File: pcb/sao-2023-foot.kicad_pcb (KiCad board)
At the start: 2 copper layers, 38.1 x 71.9 mm, 6 parts, among them J1 Conn_02x03_Odd_Even

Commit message: Now with KUBERNETES!
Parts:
- removed the G*** at (148.6, 95.2)
- added G***: LOGO, sao-2023-foot:foot_outline_edge, F.Cu at (148.6, 95.1)
- added G***: LOGO, sao-2023-foot:toes, F.Cu at (148.6, 95.0)
- moved R1 1.09 mm to (145.1, 95.0)
- moved D1 0.26 mm to (147.9, 78.3)
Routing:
- net 3V3: track 0.00 -> 22.0 mm
- net Net-(D1-A): track 0.00 -> 15.2 mm
- added copper zone on B.Cu, net GND
- added copper zone on F.Cu, net GND
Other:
- outline, holes or cut-outs redrawn

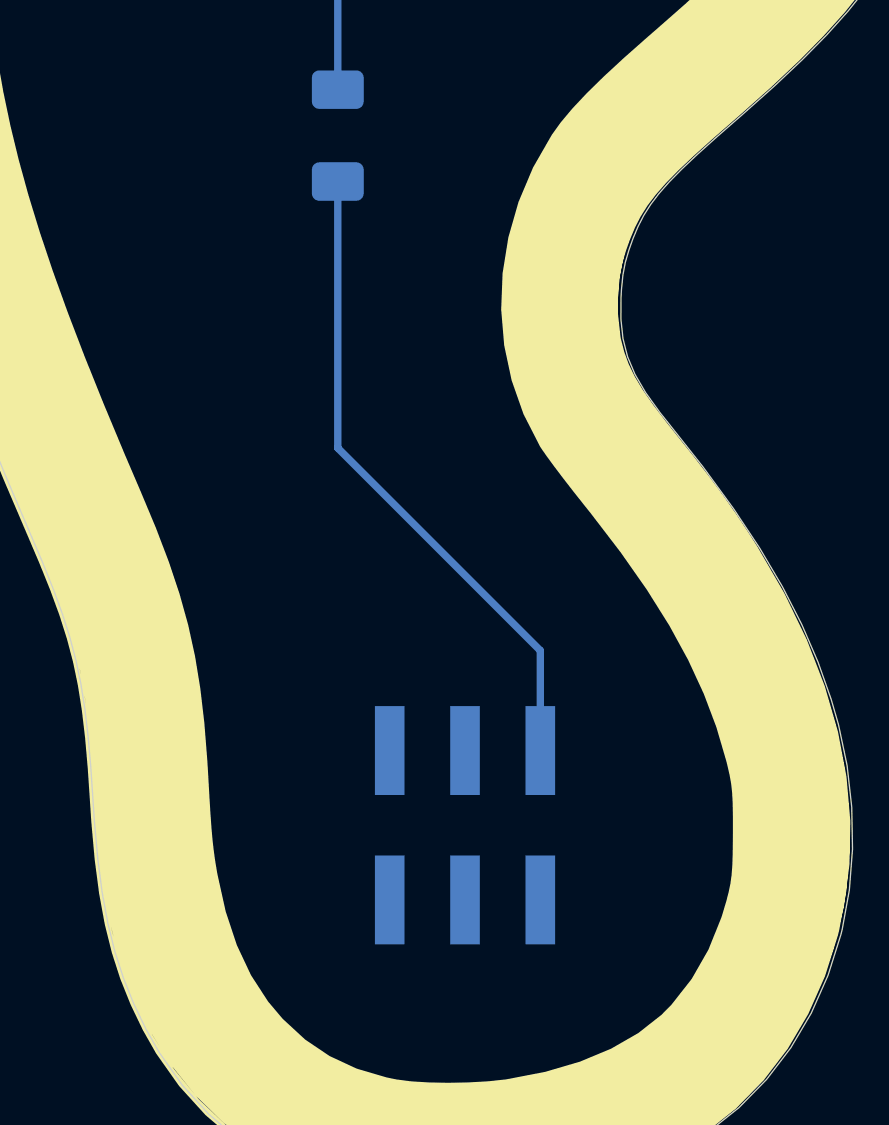
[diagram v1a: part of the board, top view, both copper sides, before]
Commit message: Corrected SAO Connector (#4)
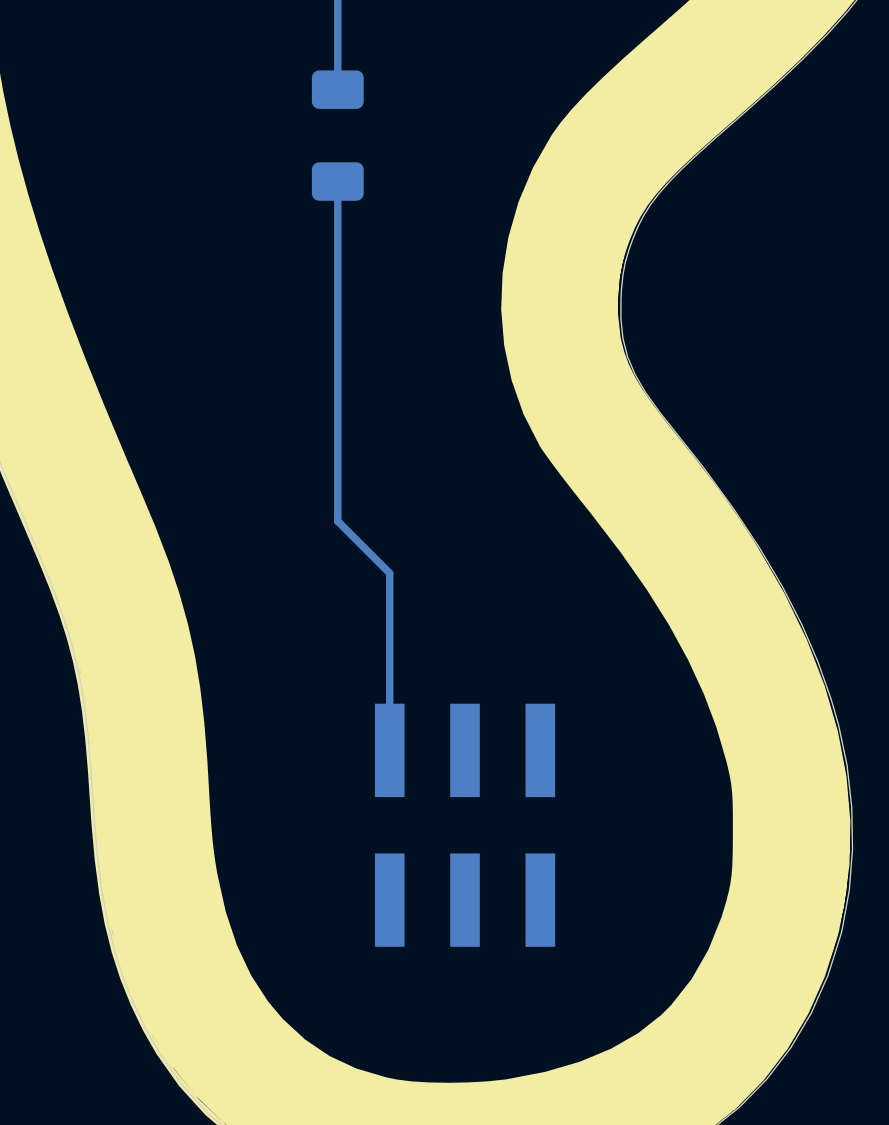
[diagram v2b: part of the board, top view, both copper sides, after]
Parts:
- J1: footprint Connector_PinSocket_2.54mm:PinSocket_2x03_P2.54mm_Vertical_SMD -> Connector_PinHeader_2.54mm:PinHeader_2x03_P2.54mm_Vertical_SMD
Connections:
- J1 pad 1: 3V3 -> unconnected-(J1-Pin_1-Pad1)
- J1 pad 2: GND -> unconnected-(J1-Pin_2-Pad2)
- J1 pad 5: unconnected-(J1-Pin_5-Pad5) -> GND
- J1 pad 6: unconnected-(J1-Pin_6-Pad6) -> 3V3
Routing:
- net 3V3: track 22.0 -> 19.9 mm
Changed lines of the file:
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@@
   (net 4 "unconnected-(J1-Pin_3-Pad3)")
   (net 5 "unconnected-(J1-Pin_4-Pad4)")
-  (net 6 "unconnected-(J1-Pin_5-Pad5)")
-  (net 7 "unconnected-(J1-Pin_6-Pad6)")
+  (net 6 "unconnected-(J1-Pin_1-Pad1)")
+  (net 7 "unconnected-(J1-Pin_2-Pad2)")
   (footprint "sao-2023-foot:foot_outline_edge" (layer "F.Cu")
     (at 148.6154 95.0722)
@@
     )
   )
-  (footprint "Connector_PinSocket_2.54mm:PinSocket_2x03_P2.54mm_Vertical_SMD" (layer "B.Cu")
+  (footprint "Connector_PinHeader_2.54mm:PinHeader_2x03_P2.54mm_Vertical_SMD" (layer "B.Cu")
     (at 149.4282 118.3132 90)
-    (descr "surface-mounted straight socket strip, 2x03, 2.54mm pitch, double cols (from Kicad 4.0.7), script generated")
-    (tags "Surface mounted socket strip SMD 2x03 2.54mm double row")
+    (descr "surface-mounted straight pin header, 2x03, 2.54mm pitch, double rows")
+    (tags "Surface mounted pin header SMD 2x03 2.54mm double row")
     (property "Sheetfile" "sao-2023-foot.kicad_sch")
     (property "Sheetname" "")
@@
     (property "ki_keywords" "connector")
     (attr smd)
-    (fp_text reference "J1" (at 0 5.31 -90) (layer "B.SilkS") hide
+    (fp_text reference "J1" (at 0 4.87 270) (layer "B.SilkS") hide
         (effects (font (size 1 1) (thickness 0.15)) (justify mirror))
     )
-    (fp_text value "Conn_02x03_Odd_Even" (at 0 -5.31 -90) (layer "B.Fab")
+    (fp_text value "Conn_02x03_Odd_Even" (at 0 -4.87 270) (layer "B.Fab")
         (effects (font (size 1 1) (thickness 0.15)) (justify mirror))
     )
@@
         (effects (font (size 1 1) (thickness 0.15)) (justify mirror))
     )
-    (fp_line (start -4.55 -4.3) (end -4.55 4.35)
+    (fp_line (start -5.9 -4.35) (end 5.9 -4.35)
       (stroke (width 0.05) (type solid)) (layer "B.CrtYd"))
-    (fp_line (start -4.55 4.35) (end 4.5 4.35)
+    (fp_line (start -5.9 4.35) (end -5.9 -4.35)
       (stroke (width 0.05) (type solid)) (layer "B.CrtYd"))
-    (fp_line (start 4.5 -4.3) (end -4.55 -4.3)
+    (fp_line (start 5.9 -4.35) (end 5.9 4.35)
       (stroke (width 0.05) (type solid)) (layer "B.CrtYd"))
-    (fp_line (start 4.5 4.35) (end 4.5 -4.3)
+    (fp_line (start 5.9 4.35) (end -5.9 4.35)
       (stroke (width 0.05) (type solid)) (layer "B.CrtYd"))
-    (fp_line (start -3.92 -2.86) (end -3.92 -2.22)
-      (stroke (width 0.1) (type solid)) (layer "B.Fab"))
-    (fp_line (start -3.92 -2.22) (end -2.54 -2.22)
-      (stroke (width 0.1) (type solid)) (layer "B.Fab"))
-    (fp_line (start -3.92 -0.32) (end -3.92 0.32)
-      (stroke (width 0.1) (type solid)) (layer "B.Fab"))
-    (fp_line (start -3.92 0.32) (end -2.54 0.32)
-      (stroke (width 0.1) (type solid)) (layer "B.Fab"))
-    (fp_line (start -3.92 2.22) (end -3.92 2.86)
-      (stroke (width 0.1) (type solid)) (layer "B.Fab"))
-    (fp_line (start -3.92 2.86) (end -2.54 2.86)
-      (stroke (width 0.1) (type solid)) (layer "B.Fab"))
-    (fp_line (start -2.54 -3.81) (end -2.54 3.81)
-      (stroke (width 0.1) (type solid)) (layer "B.Fab"))
-    (fp_line (start -2.54 -2.86) (end -3.92 -2.86)
-      (stroke (width 0.1) (type solid)) (layer "B.Fab"))
-    (fp_line (start -2.54 -0.32) (end -3.92 -0.32)
-      (stroke (width 0.1) (type solid)) (layer "B.Fab"))
-    (fp_line (start -2.54 2.22) (end -3.92 2.22)
-      (stroke (width 0.1) (type solid)) (layer "B.Fab"))
-    (fp_line (start -2.54 3.81) (end 1.54 3.81)
-      (stroke (width 0.1) (type solid)) (layer "B.Fab"))
-    (fp_line (start 1.54 3.81) (end 2.54 2.81)
+    (fp_line (start -3.6 -2.86) (end -2.54 -2.86)
+      (stroke (width 0.1) (type solid)) (layer "B.Fab"))
+    (fp_line (start -3.6 -2.22) (end -3.6 -2.86)
+      (stroke (width 0.1) (type solid)) (layer "B.Fab"))
+    (fp_line (start -3.6 -0.32) (end -2.54 -0.32)
+      (stroke (width 0.1) (type solid)) (layer "B.Fab"))
+    (fp_line (start -3.6 0.32) (end -3.6 -0.32)
+      (stroke (width 0.1) (type solid)) (layer "B.Fab"))
+    (fp_line (start -3.6 2.22) (end -2.54 2.22)
+      (stroke (width 0.1) (type solid)) (layer "B.Fab"))
+    (fp_line (start -3.6 2.86) (end -3.6 2.22)
+      (stroke (width 0.1) (type solid)) (layer "B.Fab"))
+    (fp_line (start -2.54 -3.81) (end -2.54 2.86)
+      (stroke (width 0.1) (type solid)) (layer "B.Fab"))
+    (fp_line (start -2.54 -2.22) (end -3.6 -2.22)
+      (stroke (width 0.1) (type solid)) (layer "B.Fab"))
+    (fp_line (start -2.54 0.32) (end -3.6 0.32)
+      (stroke (width 0.1) (type solid)) (layer "B.Fab"))
+    (fp_line (start -2.54 2.86) (end -3.6 2.86)
+      (stroke (width 0.1) (type solid)) (layer "B.Fab"))
+    (fp_line (start -2.54 2.86) (end -1.59 3.81)
+      (stroke (width 0.1) (type solid)) (layer "B.Fab"))
+    (fp_line (start -1.59 3.81) (end 2.54 3.81)
       (stroke (width 0.1) (type solid)) (layer "B.Fab"))
     (fp_line (start 2.54 -3.81) (end -2.54 -3.81)
       (stroke (width 0.1) (type solid)) (layer "B.Fab"))
-    (fp_line (start 2.54 -2.22) (end 3.92 -2.22)
-      (stroke (width 0.1) (type solid)) (layer "B.Fab"))
-    (fp_line (start 2.54 0.32) (end 3.92 0.32)
-      (stroke (width 0.1) (type solid)) (layer "B.Fab"))
-    (fp_line (start 2.54 2.81) (end 2.54 -3.81)
-      (stroke (width 0.1) (type solid)) (layer "B.Fab"))
-    (fp_line (start 2.54 2.86) (end 3.92 2.86)
-      (stroke (width 0.1) (type solid)) (layer "B.Fab"))
-    (fp_line (start 3.92 -2.86) (end 2.54 -2.86)
-      (stroke (width 0.1) (type solid)) (layer "B.Fab"))
-    (fp_line (start 3.92 -2.22) (end 3.92 -2.86)
-      (stroke (width 0.1) (type solid)) (layer "B.Fab"))
-    (fp_line (start 3.92 -0.32) (end 2.54 -0.32)
-      (stroke (width 0.1) (type solid)) (layer "B.Fab"))
-    (fp_line (start 3.92 0.32) (end 3.92 -0.32)
-      (stroke (width 0.1) (type solid)) (layer "B.Fab"))
-    (fp_line (start 3.92 2.22) (end 2.54 2.22)
-      (stroke (width 0.1) (type solid)) (layer "B.Fab"))
-    (fp_line (start 3.92 2.86) (end 3.92 2.22)
-      (stroke (width 0.1) (type solid)) (layer "B.Fab"))
-    (pad "1" smd rect (at 2.52 2.54 90) (size 3 1) (layers "B.Cu" "B.Paste" "B.Mask")
-      (net 3 "3V3") (pinfunction "Pin_1") (pintype "passive"))
-    (pad "2" smd rect (at -2.52 2.54 90) (size 3 1) (layers "B.Cu" "B.Paste" "B.Mask")
-      (net 1 "GND") (pinfunction "Pin_2") (pintype "passive"))
-    (pad "3" smd rect (at 2.52 0 90) (size 3 1) (layers "B.Cu" "B.Paste" "B.Mask")
+    (fp_line (start 2.54 -2.22) (end 3.6 -2.22)
+      (stroke (width 0.1) (type solid)) (layer "B.Fab"))
+    (fp_line (start 2.54 0.32) (end 3.6 0.32)
+      (stroke (width 0.1) (type solid)) (layer "B.Fab"))
+    (fp_line (start 2.54 2.86) (end 3.6 2.86)
+      (stroke (width 0.1) (type solid)) (layer "B.Fab"))
+    (fp_line (start 2.54 3.81) (end 2.54 -3.81)
+      (stroke (width 0.1) (type solid)) (layer "B.Fab"))
+    (fp_line (start 3.6 -2.86) (end 2.54 -2.86)
+      (stroke (width 0.1) (type solid)) (layer "B.Fab"))
+    (fp_line (start 3.6 -2.22) (end 3.6 -2.86)
+      (stroke (width 0.1) (type solid)) (layer "B.Fab"))
+    (fp_line (start 3.6 -0.32) (end 2.54 -0.32)
+      (stroke (width 0.1) (type solid)) (layer "B.Fab"))
+    (fp_line (start 3.6 0.32) (end 3.6 -0.32)
+      (stroke (width 0.1) (type solid)) (layer "B.Fab"))
+    (fp_line (start 3.6 2.22) (end 2.54 2.22)
+      (stroke (width 0.1) (type solid)) (layer "B.Fab"))
+    (fp_line (start 3.6 2.86) (end 3.6 2.22)
+      (stroke (width 0.1) (type solid)) (layer "B.Fab"))
+    (pad "1" smd rect (at -2.525 2.54 90) (size 3.15 1) (layers "B.Cu" "B.Paste" "B.Mask")
+      (net 6 "unconnected-(J1-Pin_1-Pad1)") (pinfunction "Pin_1") (pintype "passive"))
+    (pad "2" smd rect (at 2.525 2.54 90) (size 3.15 1) (layers "B.Cu" "B.Paste" "B.Mask")
+      (net 7 "unconnected-(J1-Pin_2-Pad2)") (pinfunction "Pin_2") (pintype "passive"))
+    (pad "3" smd rect (at -2.525 0 90) (size 3.15 1) (layers "B.Cu" "B.Paste" "B.Mask")
       (net 4 "unconnected-(J1-Pin_3-Pad3)") (pinfunction "Pin_3") (pintype "passive"))
-    (pad "4" smd rect (at -2.52 0 90) (size 3 1) (layers "B.Cu" "B.Paste" "B.Mask")
+    (pad "4" smd rect (at 2.525 0 90) (size 3.15 1) (layers "B.Cu" "B.Paste" "B.Mask")
       (net 5 "unconnected-(J1-Pin_4-Pad4)") (pinfunction "Pin_4") (pintype "passive"))
-    (pad "5" smd rect (at 2.52 -2.54 90) (size 3 1) (layers "B.Cu" "B.Paste" "B.Mask")
-      (net 6 "unconnected-(J1-Pin_5-Pad5)") (pinfunction "Pin_5") (pintype "passive"))
-    (pad "6" smd rect (at -2.52 -2.54 90) (size 3 1) (layers "B.Cu" "B.Paste" "B.Mask")
-      (net 7 "unconnected-(J1-Pin_6-Pad6)") (pinfunction "Pin_6") (pintype "passive"))
-    (model "${KICAD6_3DMODEL_DIR}/Connector_PinSocket_2.54mm.3dshapes/PinSocket_2x03_P2.54mm_Vertical_SMD.wrl"
+    (pad "5" smd rect (at -2.525 -2.54 90) (size 3.15 1) (layers "B.Cu" "B.Paste" "B.Mask")
+      (net 1 "GND") (pinfunction "Pin_5") (pintype "passive"))
+    (pad "6" smd rect (at 2.525 -2.54 90) (size 3.15 1) (layers "B.Cu" "B.Paste" "B.Mask")
+      (net 3 "3V3") (pinfunction "Pin_6") (pintype "passive"))
+    (model "${KICAD6_3DMODEL_DIR}/Connector_PinHeader_2.54mm.3dshapes/PinHeader_2x03_P2.54mm_Vertical_SMD.wrl"
       (offset (xyz 0 0 0))
       (scale (xyz 1 1 1))
@@
     (stroke (width 0.2) (type solid)) (fill solid) (layer "B.Mask"))
   (segment (start 145.1356 78.3336) (end 145.1356 93.4968) (width 0.25) (layer "B.Cu") (net 2))
-  (segment (start 151.9682 112.4204) (end 145.1356 105.5878) (width 0.25) (layer "B.Cu") (net 3))
-  (segment (start 151.9682 115.7932) (end 151.9682 112.4204) (width 0.25) (layer "B.Cu") (net 3))
-  (segment (start 145.1356 105.5878) (end 145.1356 96.5968) (width 0.25) (layer "B.Cu") (net 3))
+  (segment (start 145.1356 108.0606) (end 146.8882 109.8132) (width 0.25) (layer "B.Cu") (net 3))
+  (segment (start 146.8882 109.8132) (end 146.8882 115.7932) (width 0.25) (layer "B.Cu") (net 3))
+  (segment (start 145.1356 96.5968) (end 145.1356 108.0606) (width 0.25) (layer "B.Cu") (net 3))
   (zone (net 1) (net_name "GND") (layer "F.Cu") (hatch edge 0.5)
     (connect_pads (clearance 0))
